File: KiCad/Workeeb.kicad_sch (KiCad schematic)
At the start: 201 parts, among them U1 EFM32HG322F64G-C-QFP48

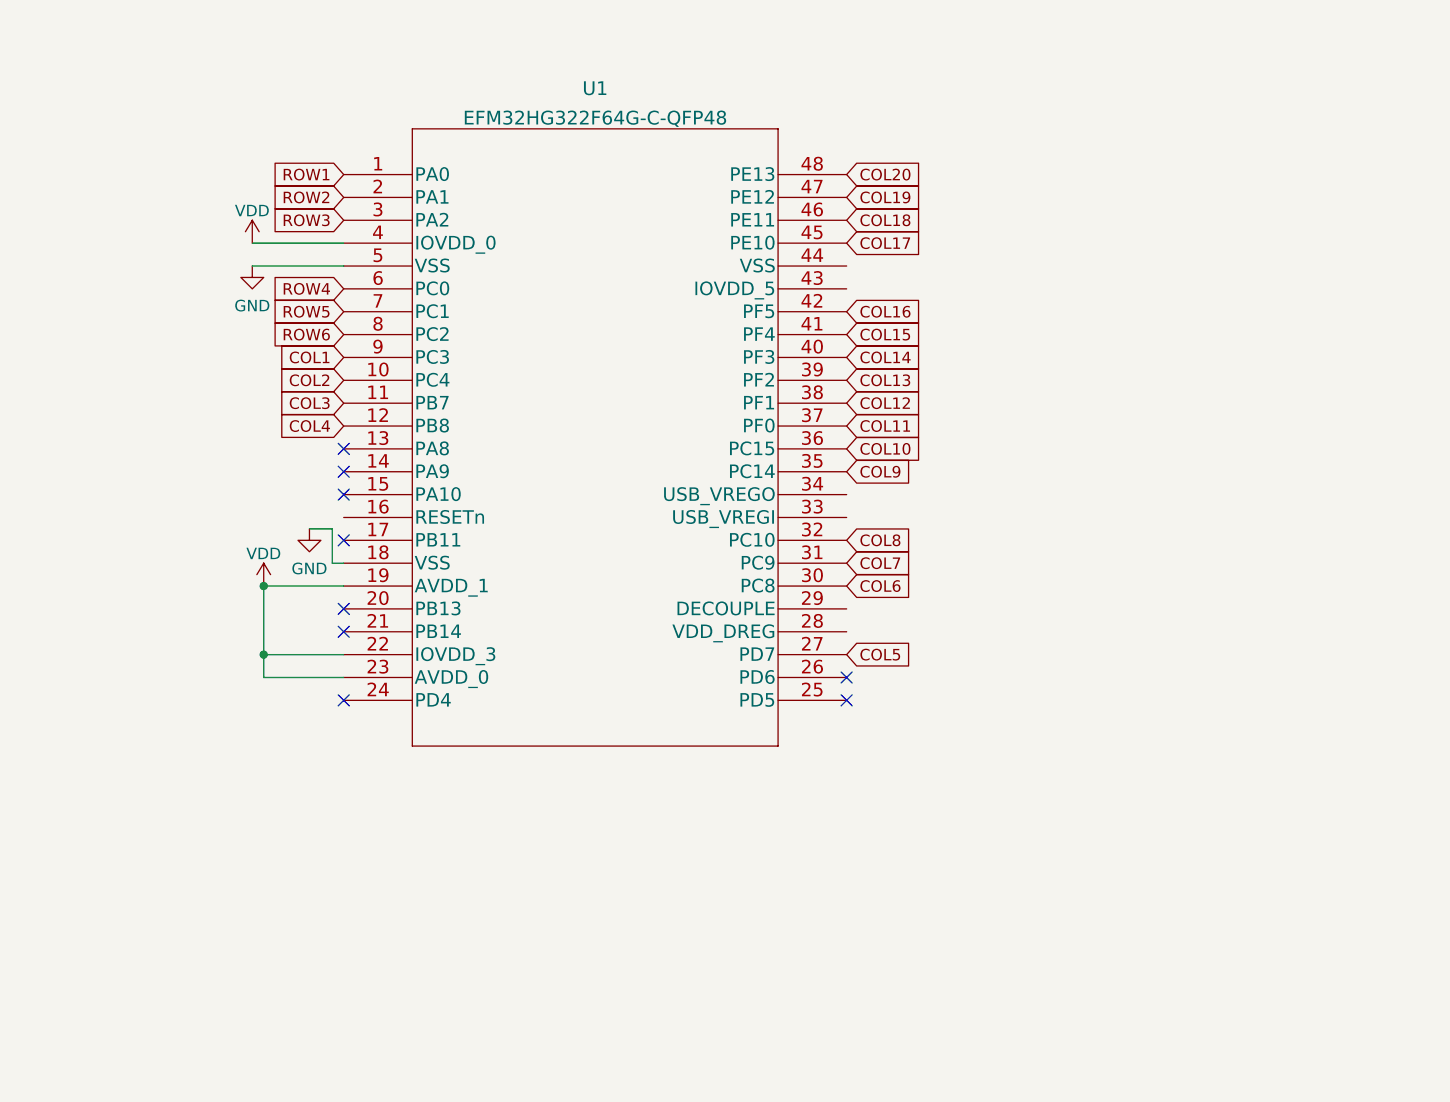
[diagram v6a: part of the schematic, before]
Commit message: Clean up MCU pwr connections
Start laying out decoupling caps
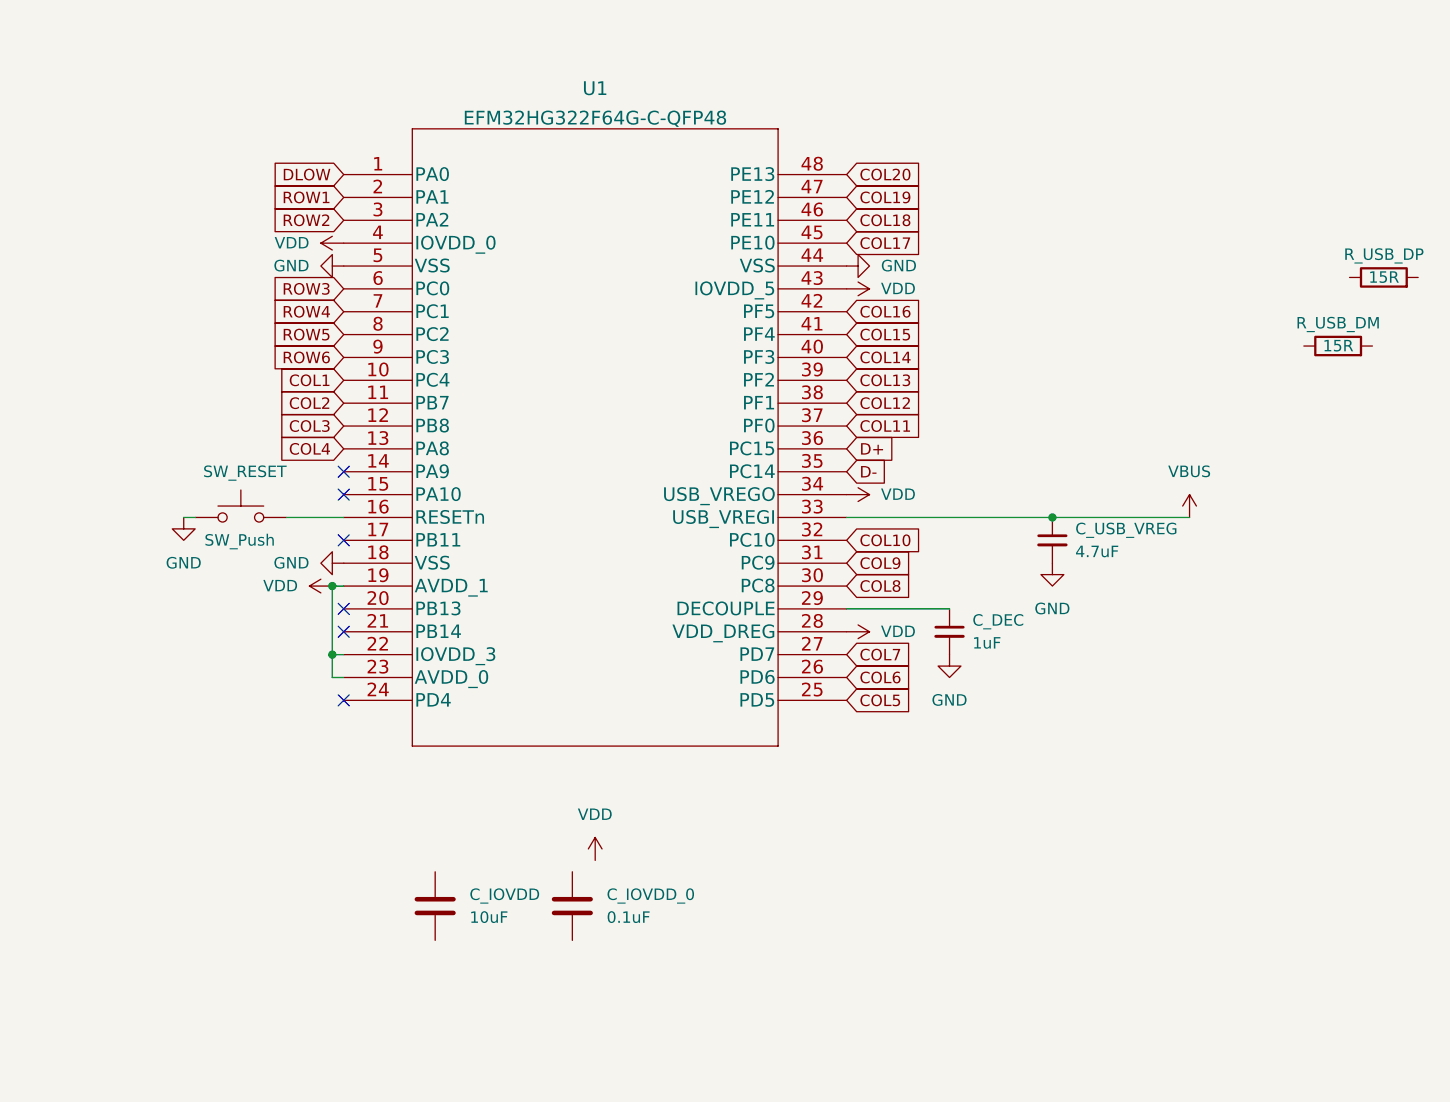
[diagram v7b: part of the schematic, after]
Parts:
- added C_DEC: 1uF, symbol Device:C_Small
- added C_IOVDD: 10uF, symbol Device:C
- added C_IOVDD_0: 0.1uF, symbol Device:C
- added C_USB_VREG: 4.7uF, symbol Device:C_Small
- added R_USB_DM, R_USB_DP: 15R, symbol Device:R
- added SW_RESET: SW_Push, symbol Switch:SW_Push
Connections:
- net COL1: now also U1.10 (PC4); no longer U1.9 (PC3)
- net COL10: now also U1.32 (PC10); no longer U1.36 (PC15)
- net COL2: now also U1.11 (PB7); no longer U1.10 (PC4)
- net COL3: now also U1.12 (PB8); no longer U1.11 (PB7)
- net COL4: now also U1.13 (PA8); no longer U1.12 (PB8)
- net COL5: now also U1.25 (PD5); no longer U1.27 (PD7)
- net COL6: now also U1.26 (PD6); no longer U1.30 (PC8)
- net COL7: now also U1.27 (PD7); no longer U1.31 (PC9)
- net COL8: now also U1.30 (PC8); no longer U1.32 (PC10)
- net COL9: now also U1.31 (PC9); no longer U1.35 (PC14)
- net GND: now also U1.44 (VSS), C_DEC.2, C_USB_VREG.2, SW_RESET.1
- net ROW1: now also U1.2 (PA1); no longer U1.1 (PA0)
- net ROW2: now also U1.3 (PA2); no longer U1.2 (PA1)
- net ROW3: now also U1.6 (PC0); no longer U1.3 (PA2)
- net ROW4: now also U1.7 (PC1); no longer U1.6 (PC0)
- net ROW5: now also U1.8 (PC2); no longer U1.7 (PC1)
- net ROW6: now also U1.9 (PC3); no longer U1.8 (PC2)
- net VDD: now also U1.28 (VDD_DREG), U1.34 (USB_VREGO), U1.43 (IOVDD_5)
- net at U1.16 (RESETn): now also SW_RESET.2
- net at U1.29 (DECOUPLE): now also C_DEC.1
- net VBUS: now reaches U1.33 (USB_VREGI)
- net VBUS: now also C_USB_VREG.1
- new net D+: U1.36 (PC15)
- new net D-: U1.35 (PC14)
- new net DLOW: U1.1 (PA0)
- no-connect marks 9 -> 6

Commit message: Finish up schematic first draft
Mess around a bit with PCB
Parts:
- removed C_USB_VREG: 4.7uF, symbol Device:C_Small
- removed R_USB_DM, R_USB_DP: 15R, symbol Device:R
- added C_AVDD1, C_VDD1: 10uF, Capacitor_SMD:C_0805_2012Metric, symbol Device:C
- added C_AVDD_0, C_AVDD_1: 10nF, Capacitor_SMD:C_0805_2012Metric, symbol Device:C
- added C_DEC2, C_VREGO1: 1uF, Capacitor_SMD:C_0805_2012Metric, symbol Device:C
- added C_IOVDD_3, C_IOVDD_5, C_VDD_1: 0.1uF, Capacitor_SMD:C_0805_2012Metric, symbol Device:C
- added C_RESET1: 100nF, Capacitor_SMD:C_0805_2012Metric, symbol Device:C
- added C_VREGI1: 4.7uF, Capacitor_SMD:C_0805_2012Metric, symbol Device:C
- added FB_VBUS1: FB, Inductor_SMD:L_0805_2012Metric, symbol Device:FerriteBead_Small
- added J1: USB_C_Receptacle_USB2.0, Connector_USB:USB_C_Receptacle_GCT_USB4085, symbol Connector:USB_C_Receptacle_USB2.0
- added R_CC1, R_CC2: 5.1k, Resistor_SMD:R_0805_2012Metric, symbol Device:R
- added R_D+1, R_D-1: 15, Resistor_SMD:R_0805_2012Metric, symbol Device:R
- added R_DMPU1: 4.7K, Resistor_SMD:R_0805_2012Metric, symbol Device:R
- added R_RESET1: 100, Resistor_SMD:R_0805_2012Metric, symbol Device:R
- C_DEC1: renamed from C_DEC; footprint (none) -> Capacitor_SMD:C_0805_2012Metric
- C_IOVDD1: renamed from C_IOVDD; footprint (none) -> Capacitor_SMD:C_0805_2012Metric
- C_IOVDD_0: footprint (none) -> Capacitor_SMD:C_0805_2012Metric
- SW_RESET1: renamed from SW_RESET; footprint (none) -> random-keyboard-parts:PushButton_6x6mm_TH_Pretty
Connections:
- net D+: now also R_D+1.2
- net D-: now also R_D-1.2
- net GND: now also C_IOVDD1.2, C_IOVDD_0.2, C_AVDD1.2, C_AVDD_0.2, C_AVDD_1.2, C_DEC2.2, C_IOVDD_3.2, C_IOVDD_5.2, C_RESET1.2, C_VDD1.2, C_VDD_1.2, C_VREGI1.2, C_VREGO1.2, J1.A1 (GND), J1.A12 (GND), J1.B1 (GND), J1.B12 (GND), J1.S1 (SHIELD), R_CC1.2, R_CC2.2, R_RESET1.1; no longer SW_RESET1.1
- net VBUS: now also C_VREGI1.1, FB_VBUS1.2
- net VDD: now also C_IOVDD1.1, C_IOVDD_0.1, C_AVDD1.1, C_AVDD_0.1, C_AVDD_1.1, C_DEC2.1, C_IOVDD_3.1, C_IOVDD_5.1, C_VDD1.1, C_VDD_1.1, C_VREGO1.1
- net RESET: now reaches SW_RESET1.2, U1.16 (RESETn)
- net RESET: now also C_RESET1.1
- net DLOW renamed DMPU
- net DMPU: now also R_DMPU1.2
- new net: J1.A7 (D-), J1.B7 (D-), R_D-1.1
- new net: J1.B5 (CC2), R_CC2.1
- new net: FB_VBUS1.1, J1.A4 (VBUS), J1.A9 (VBUS), J1.B4 (VBUS), J1.B9 (VBUS)
- new net: R_RESET1.2, SW_RESET1.1
- new net: J1.A6 (D+), J1.B6 (D+), R_D+1.1, R_DMPU1.1
- new net: J1.A5 (CC1), R_CC1.1
- no-connect marks 6 -> 8
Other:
- moved on the sheet: C_IOVDD1, C_IOVDD_0, SW_RESET1
